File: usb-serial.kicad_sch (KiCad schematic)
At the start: 28 parts, among them J1 Conn_02x03_Odd_Even, U1 ACPL-M50L, U2 ACPL-M50L, U3 USBLC6-2SC6, U4 74LVC00, U6 Interface_USB_CP2102N-A01-GQF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

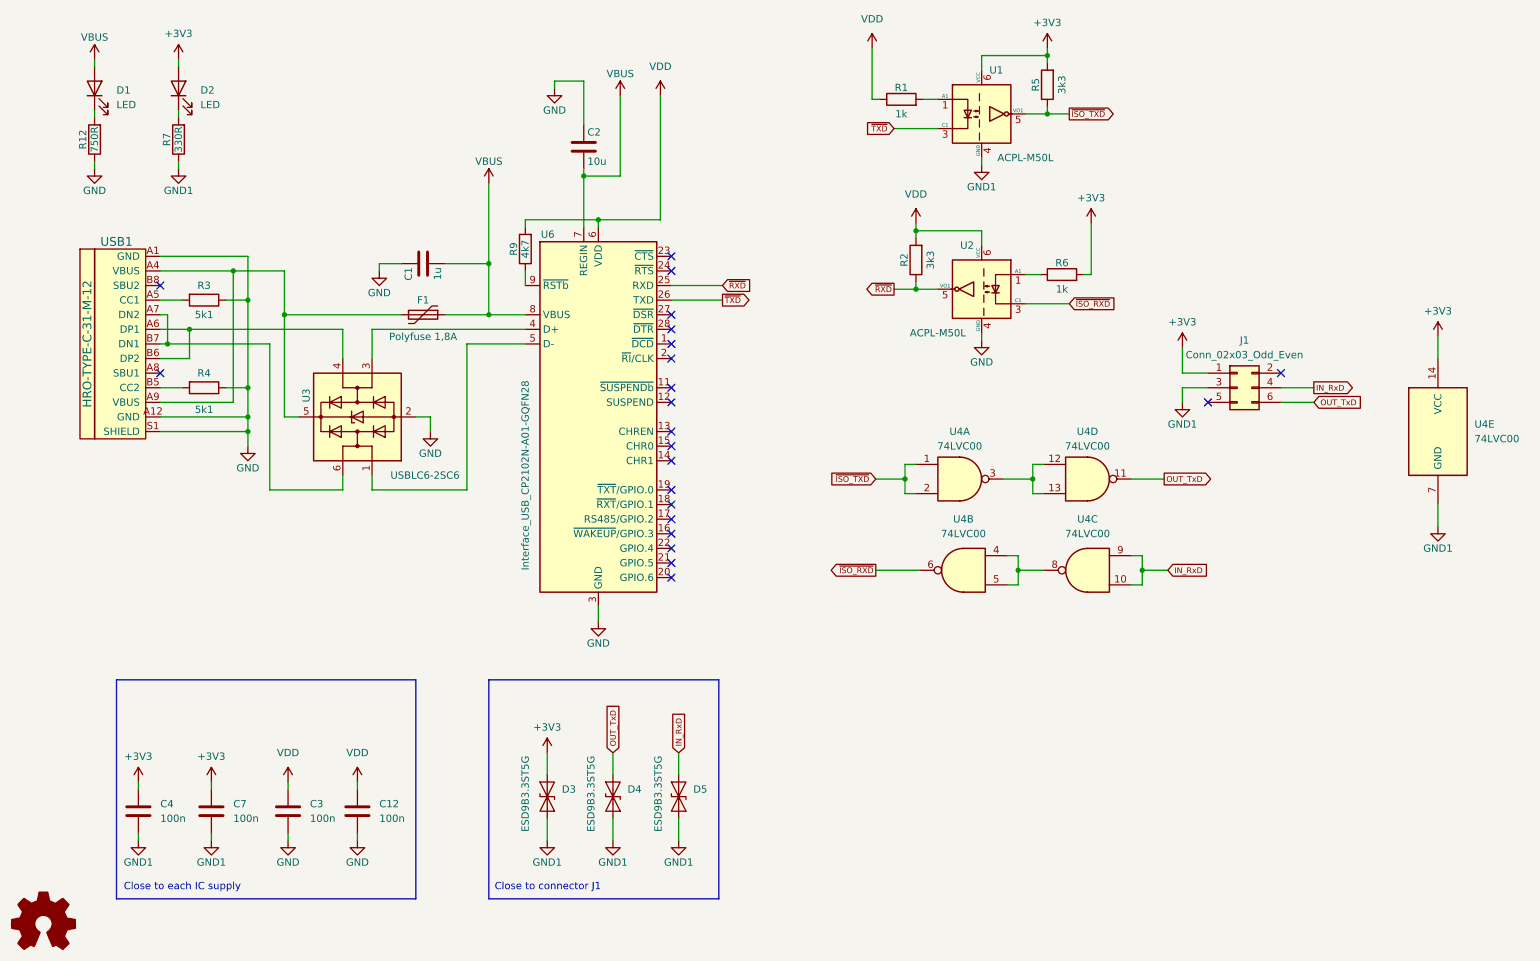
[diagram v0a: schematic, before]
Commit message: Change to capacitive isolator
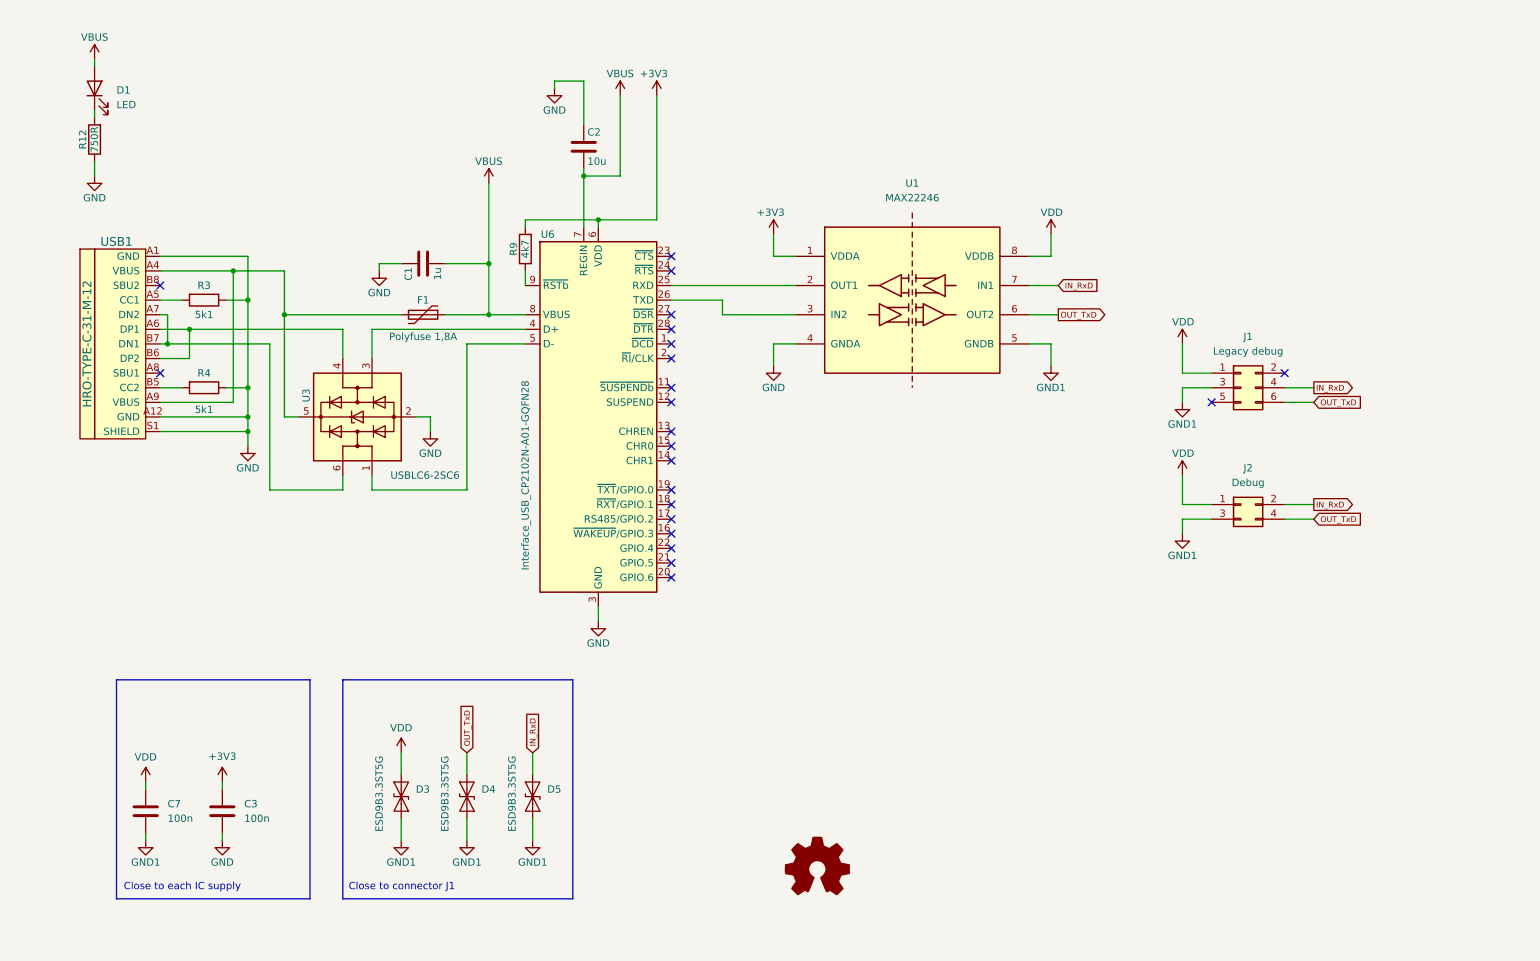
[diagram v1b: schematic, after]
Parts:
- removed C12, C4: 100n, Capacitor_SMD:C_0402_1005Metric, symbol Device:C
- removed D2: LED, LED_SMD:LED_0805_2012Metric, symbol Device:LED
- removed R1, R6: 1k, Resistor_SMD:R_0402_1005Metric, symbol Device:R
- removed R2, R5: 3k3, Resistor_SMD:R_0402_1005Metric, symbol Device:R
- removed R7: 330R, Resistor_SMD:R_0402_1005Metric, symbol Device:R
- removed U1, U2: ACPL-M50L, Package_SO:SO-5_4.4x3.6mm_P1.27mm, symbol anders:ACPL-M50L
- removed U4: 74LVC00, Package_SO:SOIC-14_3.9x8.7mm_P1.27mm, symbol 74xx:74HCT00
- added J2: Debug, Connector_JST:JST_PH_S4B-PH-SM4-TB_1x04-1MP_P2.00mm_Horizontal, symbol Connector_Generic:Conn_02x02_Odd_Even
- added U1: MAX22246, Package_SO:SOP-8_5.28x5.23mm_P1.27mm, symbol anders:MAX22246
- J1: value Conn_02x03_Odd_Even -> Legacy debug
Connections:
- net +3V3: now also C3.1, R9.2, U6.6 (VDD), U1.1 (VDDA); no longer C7.1, D3.2 (A2), J1.1 (Pin_1)
- net GND: now also U1.4 (GNDA)
- net GND1: now also J2.3 (Pin_3), U1.5 (GNDB)
- net IN_RxD: now also J2.2 (Pin_2), U1.7 (IN1)
- net OUT_TxD: now also J2.4 (Pin_4), U1.6 (OUT2)
- net VDD: now also C7.1, D3.2 (A2), J1.1 (Pin_1), J2.1 (Pin_1), U1.8 (VDDB); no longer C3.1, R9.2, U6.6 (VDD)
- net ~{RXD}: no longer names the net of U6.25 (RXD)
- net ~{RXD}: now also U1.2 (OUT1)
- net ~{TXD}: no longer names the net of U6.26 (TXD)
- net ~{TXD}: now also U1.3 (IN2)
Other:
- title: Opto isolated USB to serial 3.3V TTL  converter -> Galvanic isolated USB to serial TTL converter
- moved on the sheet: C3, C7, D3, D4, D5, J1
